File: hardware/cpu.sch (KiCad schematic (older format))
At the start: 38 parts

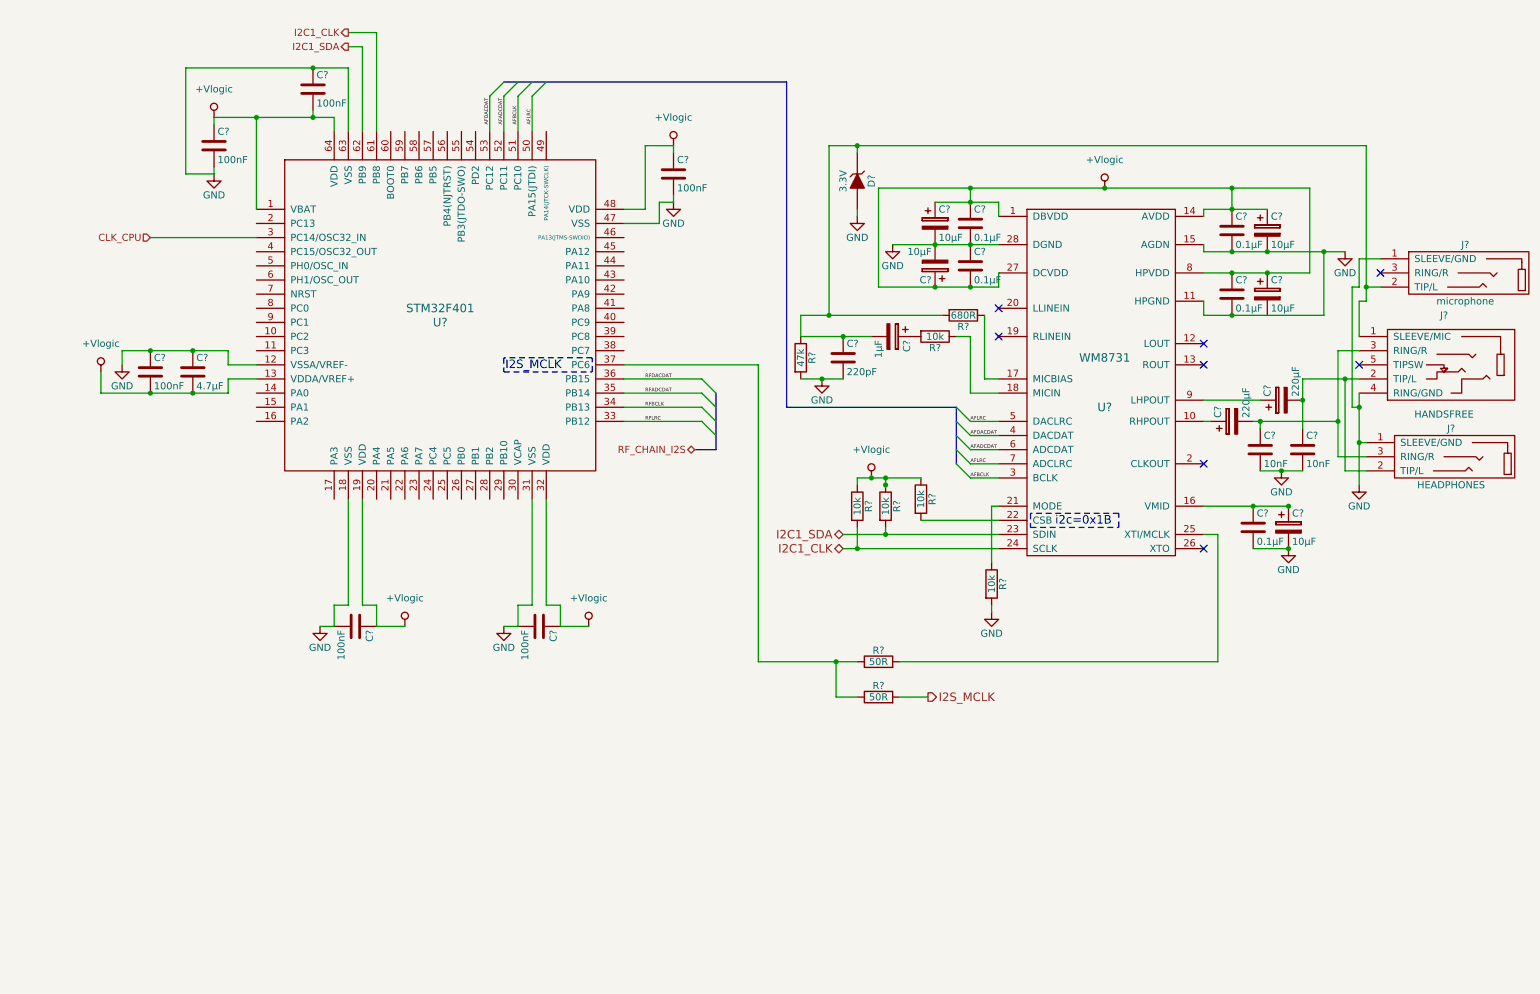
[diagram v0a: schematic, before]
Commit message: Allocated CPU some pins and made minor adjustments here and there
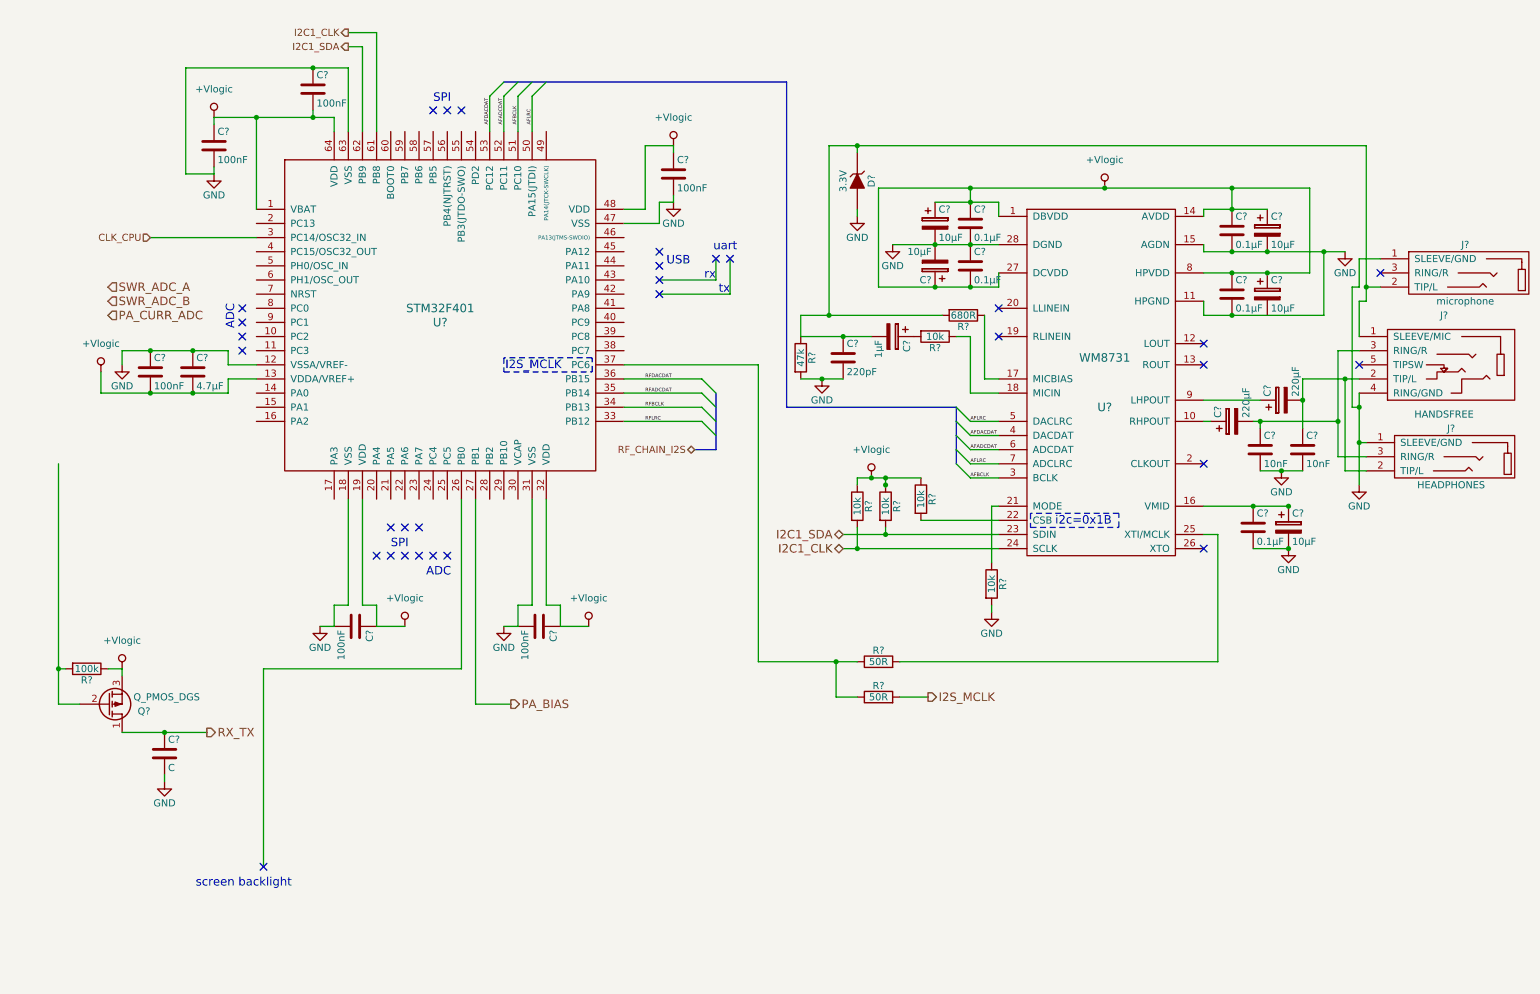
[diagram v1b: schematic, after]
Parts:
- added C?: C, symbol C
- added Q?: Q_PMOS_DGS, symbol Q_PMOS_DGS
- added R?: 100k, symbol R
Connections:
- net +Vlogic: now also Q?.3 (S), R?.1
- net GND: now also C?.2
- net PA_BIAS: now reaches U?.27 (PB1)
- new net: Q?.2 (G), R?.2
- new net RX_TX: C?.1, Q?.1 (D)
- no-connect marks 8 -> 31
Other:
- note added: "ADC"
- note added: "SPI"
- note added: "USB"
- note added: "rx"
- note added: "screen backlight"
- note added: "tx"
- note added: "uart"

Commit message: Made some minor adjustments and replotted schematic .pdf
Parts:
- added C?: 10µF, symbol C
- added D? (x3): BAT54SL, symbol D_Schottky_x2_Serial_AKC
- added P?: TX_SW_WIRE, symbol CONN_01X02
- added R?: 10k, symbol R
- added R? (x2): 100R, symbol R
- added SW?: SW_PUSH, symbol SW_PUSH
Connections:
- net +Vlogic: now also D?.2 (K), D?.2 (K), D?.2 (K), R?.1
- net GND: now also C?.2, D?.1 (A), D?.1 (A), D?.1 (A), P?.2 (P2), SW?.1
- net PA_CURR_ADC: now also U?.10 (PC2), D?.3 (common)
- net SWR_ADC_A: now also U?.8 (PC0), D?.3 (common)
- net SWR_ADC_B: now also U?.9 (PC1), D?.3 (common)
- net at U?.14 (PA0): now also C?.1, R?.1
- net at U?.15 (PA1): now also R?.2, R?.1
- net at Q?.2 (G): now also R?.2; no longer R?.2
- new net: P?.1 (P1), R?.2, R?.2, SW?.2
- no-connect marks 31 -> 29
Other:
- moved on the sheet: C?, D?, J?, Q?, R?, U?

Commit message: fixed some bugs
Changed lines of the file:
@@
 NoConn ~ 10000 2100
 Wire Wire Line
-	1900 1250 2200 1250
-Wire Wire Line
-	2200 1250 2600 1250
-Wire Wire Line
-	2600 1250 2750 1250
+	1900 1250 2750 1250
 Wire Wire Line
 	2750 1250 2750 1350
@@
 	2850 900  2850 1350
 Wire Wire Line
-	1700 900  2600 900
-Wire Wire Line
-	2600 900  2850 900
+	1700 900  2850 900
 Wire Wire Line
 	1700 900  1700 1650
@@
 	2200 3100 1600 3100
 Wire Wire Line
-	1600 3100 1600 3200
-Wire Wire Line
-	1600 3200 1350 3200
-Wire Wire Line
-	1350 3200 1050 3200
-Wire Wire Line
-	1050 3200 700  3200
+	1600 3200 1600 3100
+Wire Wire Line
+	700  3200 1600 3200
 Wire Wire Line
 	700  3200 700  3050
@@
 	850  3000 850  2900
 Wire Wire Line
-	850  2900 1050 2900
-Wire Wire Line
-	1050 2900 1350 2900
-Wire Wire Line
-	1350 2900 1600 2900
+	850  2900 1600 2900
 Wire Wire Line
 	1600 2900 1600 3000
@@
 Connection ~ 1350 3200
 Wire Wire Line
-	6700 1250 7000 1250
-Wire Wire Line
-	7000 1250 7250 1250
-Wire Wire Line
-	7250 1250 7450 1250
+	6700 1250 7450 1250
 Wire Wire Line
 	7450 950  7450 1050
 Wire Wire Line
-	7000 950  7250 950
-Wire Wire Line
-	7250 950  7450 950
+	7000 950  7450 950
 Connection ~ 7250 950
 Wire Wire Line
 	7250 950  7250 850
 Wire Wire Line
-	6600 850  7250 850
-Wire Wire Line
-	7250 850  8200 850
-Wire Wire Line
-	8200 850  9100 850
-Wire Wire Line
-	9100 850  9650 850
+	6600 850  9650 850
 Connection ~ 7000 1250
 Connection ~ 7250 1250
@@
 Connection ~ 8200 850
 Wire Wire Line
-	8900 1000 9100 1000
-Wire Wire Line
-	9100 1000 9350 1000
+	8900 1000 9350 1000
 Wire Wire Line
 	8900 1000 8900 1050
 Connection ~ 9100 1000
 Wire Wire Line
-	8900 1300 9100 1300
-Wire Wire Line
-	9100 1300 9350 1300
-Wire Wire Line
-	9350 1300 9750 1300
-Wire Wire Line
-	9750 1300 9900 1300
+	8900 1300 9900 1300
 Wire Wire Line
 	8900 1300 8900 1250
@@
 Connection ~ 9350 1300
 Wire Wire Line
-	9650 850  9650 1450
-Wire Wire Line
-	9650 1450 9350 1450
-Wire Wire Line
-	9350 1450 9100 1450
-Wire Wire Line
-	9100 1450 8900 1450
+	9650 1450 9650 850
+Wire Wire Line
+	8900 1450 9650 1450
 Connection ~ 9100 850
 Connection ~ 9350 1450
@@
 	8900 1650 8900 1750
 Wire Wire Line
-	8900 1750 9100 1750
-Wire Wire Line
-	9100 1750 9750 1750
+	8900 1750 9750 1750
 Wire Wire Line
 	9750 1750 9750 1300
@@
 Connection ~ 9100 1750
 Wire Wire Line
-	6600 1550 7000 1550
-Wire Wire Line
-	7000 1550 7250 1550
-Wire Wire Line
-	7250 1550 7450 1550
+	6600 1550 7450 1550
 Wire Wire Line
 	7450 1550 7450 1450
@@
 Connection ~ 7000 1550
 Wire Wire Line
-	6350 3300 6650 3300
-Wire Wire Line
-	6650 3300 7450 3300
+	6350 3300 7450 3300
 Wire Wire Line
 	6650 3300 6650 3250
 Wire Wire Line
-	6350 3400 6450 3400
-Wire Wire Line
-	6450 3400 7450 3400
+	6350 3400 7450 3400
 Wire Wire Line
 	6450 3400 6450 3250
@@
 Connection ~ 6650 2950
 Wire Wire Line
-	6450 2900 6550 2900
-Wire Wire Line
-	6550 2900 6650 2900
-Wire Wire Line
-	6650 2900 6900 2900
+	6450 2900 6900 2900
 Wire Wire Line
 	6450 2900 6450 2950
@@
 	7400 3100 7400 3500
 Wire Wire Line
-	5750 4200 6300 4200
-Wire Wire Line
-	6300 4200 6450 4200
+	5750 4200 6450 4200
 Wire Wire Line
 	5750 4200 5750 3000
@@
 	7250 2900 7450 2900
 Wire Bus Line
-	7150 2400 7150 2500
-Wire Bus Line
-	7150 2500 7150 2600
-Wire Bus Line
-	7150 2600 7150 2700
-Wire Bus Line
-	7150 2700 7150 2800
+	7150 2400 7150 2800
 Wire Bus Line
 	5950 2400 7150 2400
@@
 	5950 1000 5950 2400
 Wire Bus Line
-	3950 1000 4050 1000
-Wire Bus Line
-	4050 1000 4150 1000
-Wire Bus Line
-	4150 1000 4250 1000
-Wire Bus Line
-	4250 1000 5950 1000
+	3950 1000 5950 1000
 Wire Wire Line
 	2850 750  2950 750
@@
 	3050 650  3050 1350
 Wire Wire Line
-	9300 2850 9450 2850
-Wire Wire Line
-	9450 2850 9600 2850
+	9300 2850 9600 2850
 Connection ~ 9450 2850
 Wire Wire Line
 	9250 3400 9500 3400
 Wire Wire Line
-	8900 3100 9250 3100
-Wire Wire Line
-	9250 3100 9500 3100
-Wire Wire Line
-	9600 2200 9600 2350
-Wire Wire Line
-	9600 2350 9600 2550
-Wire Wire Line
-	9600 2200 9900 2200
-Wire Wire Line
-	9900 2200 10000 2200
+	8900 3100 9500 3100
+Wire Wire Line
+	9600 2200 9600 2550
+Wire Wire Line
+	9600 2200 10000 2200
 Wire Wire Line
 	9850 2000 10000 2000
 Wire Wire Line
-	9250 2500 9300 2500
-Wire Wire Line
-	9300 2500 9850 2500
-Wire Wire Line
-	9850 2000 9850 2500
-Wire Wire Line
-	9850 2500 9850 2750
+	9250 2500 9850 2500
+Wire Wire Line
+	9850 2000 9850 2750
 Wire Wire Line
 	9900 2200 9900 2850
@@
 	10000 2650 10050 2650
 Wire Wire Line
-	10000 2300 10000 2400
-Wire Wire Line
-	10000 2400 10000 2650
-Wire Wire Line
-	10000 2650 10000 2950
+	10000 2300 10000 2950
 Connection ~ 10000 2650
 Wire Wire Line
@@
 Connection ~ 10050 1550
 Wire Wire Line
-	10050 550  10050 1550
-Wire Wire Line
-	10050 1550 10050 1650
-Wire Wire Line
-	6250 550  6450 550
-Wire Wire Line
-	6450 550  10050 550
+	10050 550  10050 1650
+Wire Wire Line
+	6250 550  10050 550
 Connection ~ 9850 2500
 Wire Wire Line
@@
 	6850 1900 6850 1900
 Wire Wire Line
-	6050 1750 6250 1750
-Wire Wire Line
-	6250 1750 7050 1750
+	6050 1750 7050 1750
 Wire Wire Line
 	6050 1750 6050 1900
 Wire Wire Line
-	6050 1900 6350 1900
-Wire Wire Line
-	6350 1900 6550 1900
+	6050 1900 6550 1900
 Connection ~ 6350 1900
 $Comp
@@
 $EndComp
 Wire Wire Line
-	6050 2200 6200 2200
-Wire Wire Line
-	6200 2200 6350 2200
+	6050 2200 6350 2200
 Connection ~ 6200 2200
 Wire Wire Line
@@
 RF_CHAIN_I2S
 Wire Bus Line
-	5450 3200 5450 3300
-Wire Bus Line
-	5450 3300 5450 3400
-Wire Bus Line
-	5450 3400 5450 3500
-Wire Bus Line
-	5450 3500 5450 3600
+	5450 3200 5450 3600
 Wire Bus Line
 	5450 3600 5300 3600
@@
 	1300 5400 1300 5350
 Wire Wire Line
-	1000 5050 1300 5050
-Wire Wire Line
-	1300 5050 1550 5050
+	1000 5050 1550 5050
 Connection ~ 1300 5050
 $Comp
@@
 $EndComp
 Wire Wire Line
-	1050 3500 1100 3500
-Wire Wire Line
-	1100 3500 1350 3500
-Wire Wire Line
-	1350 3500 1400 3500
+	1050 3500 1400 3500
 Wire Wire Line
 	1350 3500 1350 3550
@@
 $EndComp
 Wire Wire Line
-	1750 3200 1750 3500
-Wire Wire Line
-	1750 3500 1750 3700
+	1750 3200 1750 3700
 Connection ~ 1750 3500
 Wire Wire Line
 	1750 4150 1750 4000
 Wire Wire Line
-	1100 4150 1350 4150
-Wire Wire Line
-	1350 4150 1750 4150
+	1100 4150 1750 4150
 Wire Wire Line
 	1100 3500 1100 3800
 Wire Wire Line
-	1100 3900 1100 4150
-Wire Wire Line
-	1100 4150 1100 4200
+	1100 3900 1100 4200
 Connection ~ 1350 4150
 Wire Wire Line
@@
 Connection ~ 1100 3500
 Wire Wire Line
-	2000 3300 2000 4450
-Wire Wire Line
-	2000 4450 2000 4500
+	2000 3300 2000 4500
 Wire Wire Line
 	4250 4100 4250 3950
@@
 	1600 2600 2200 2600
 Wire Wire Line
-	1600 800  1600 1150
-Wire Wire Line
-	1600 1150 1600 2600
+	1600 800  1600 2600
 Wire Wire Line
 	1400 2150 850  2150
@@
 $EndComp
 Wire Wire Line
-	650  800  1000 800
-Wire Wire Line
-	1000 800  1400 800
+	650  800  1400 800
 Wire Wire Line
 	1400 800  1400 850

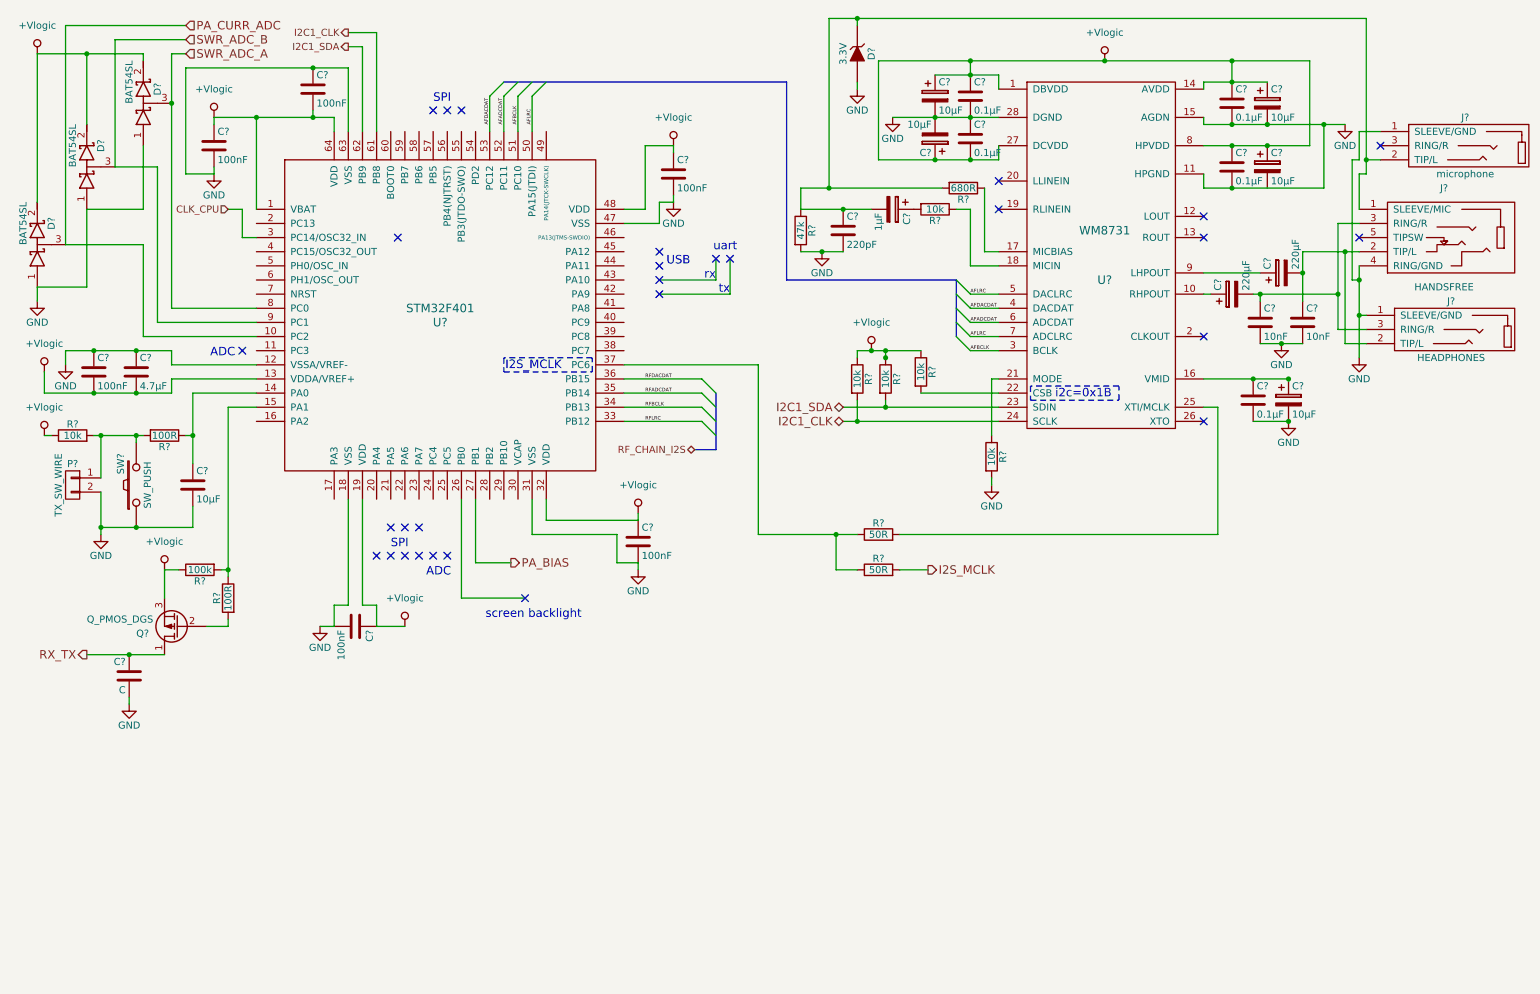
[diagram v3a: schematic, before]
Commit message: Fixed 8/11 of issue #4
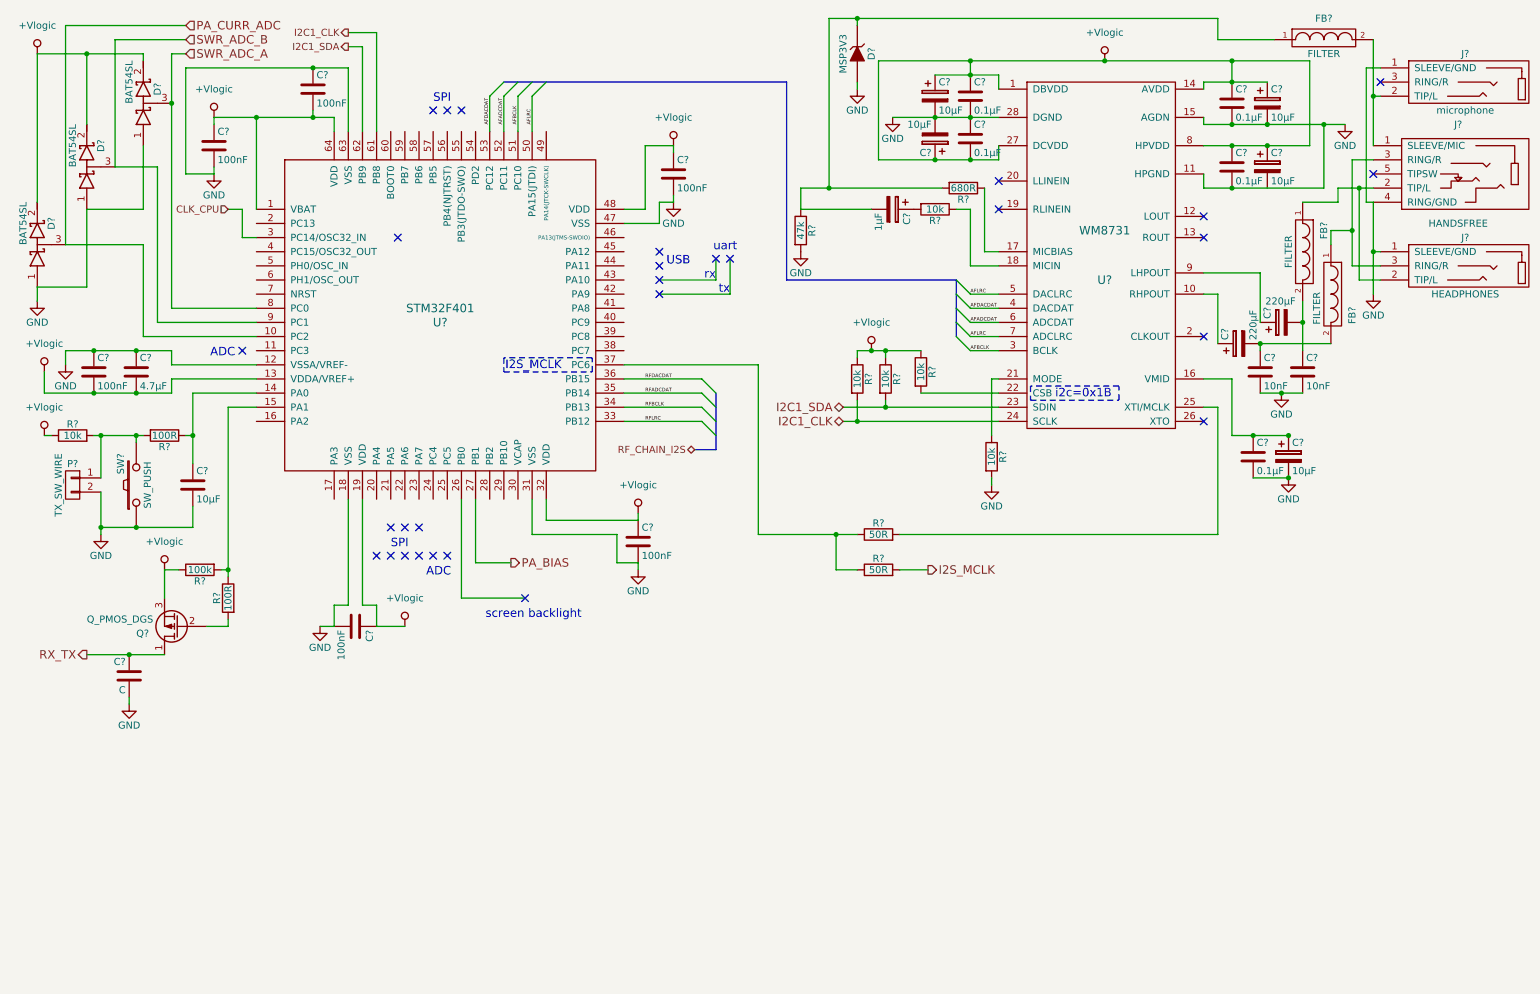
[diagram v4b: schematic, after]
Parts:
- removed C?: 220pF, symbol C
- added FB? (x3): FILTER, symbol FILTER
- D?: value 3.3V -> MSP3V3
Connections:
- net at C?.1, C?.2: now also FB?.2; no longer J?.2 (TIP/L), J?.2 (TIP/L)
- net at C?.1, C?.2: now also FB?.2; no longer J?.3 (RING/R), J?.3 (RING/R)
- net at C?.2, D?.1 (K), R?.1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: now also FB?.1; no longer J?.1 (SLEEVE/MIC), J?.2 (TIP/L)
- new net: FB?.2, J?.1 (SLEEVE/MIC), J?.2 (TIP/L)
- new net: FB?.1, J?.2 (TIP/L), J?.2 (TIP/L)
- new net: FB?.1, J?.3 (RING/R), J?.3 (RING/R)
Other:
- moved on the sheet: C?, J?
